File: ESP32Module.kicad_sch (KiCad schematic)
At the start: 5 parts, among them U4 ESP32-WROOM-32

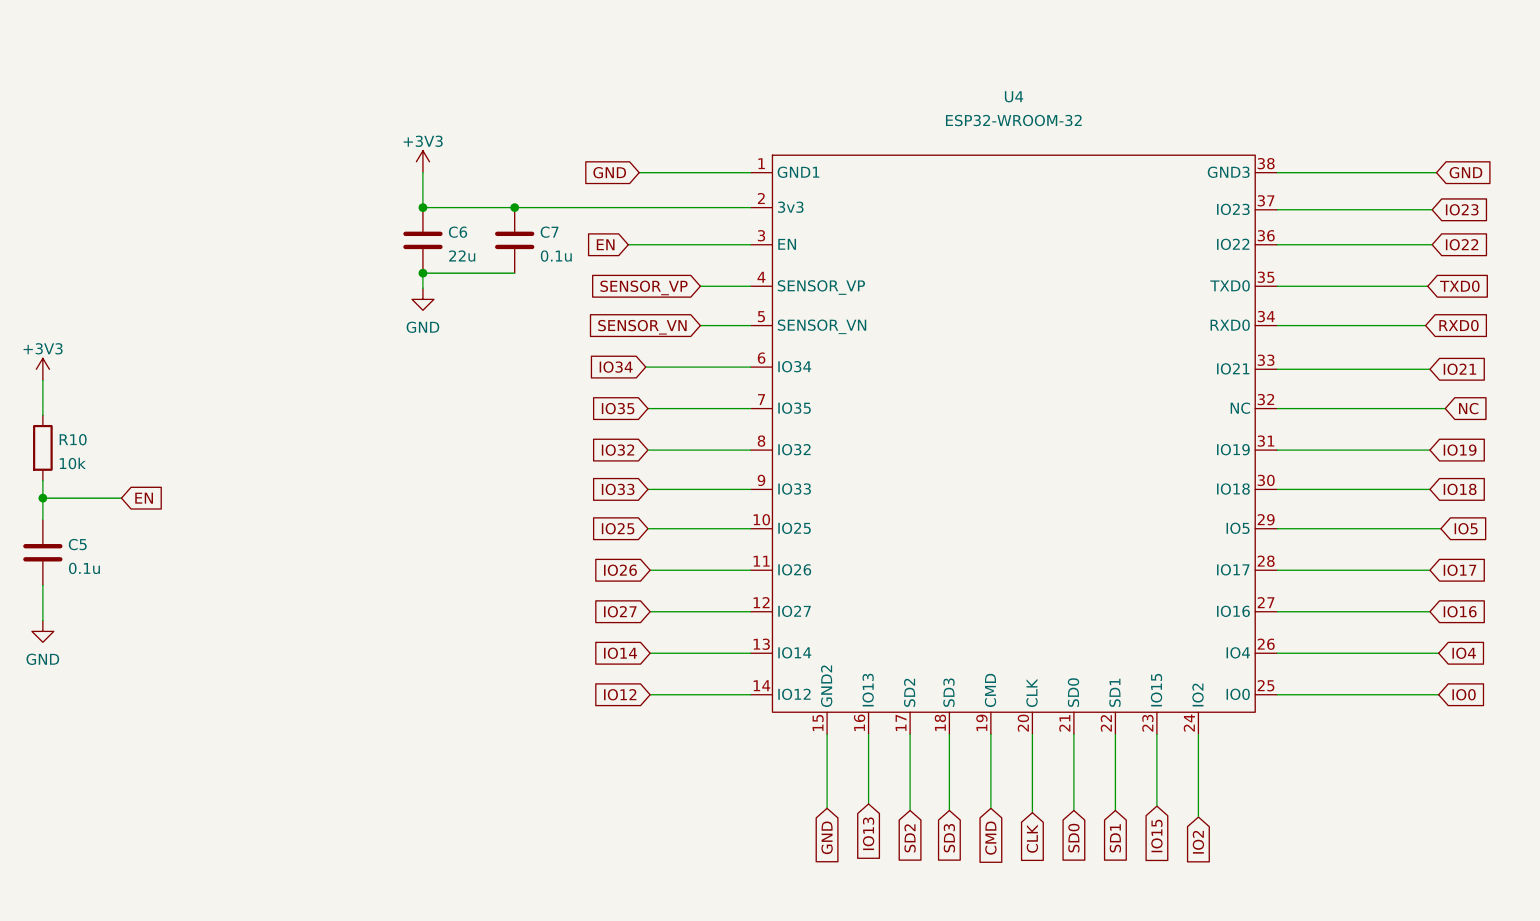
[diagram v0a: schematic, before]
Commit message: Added VOC and Optical Sensors
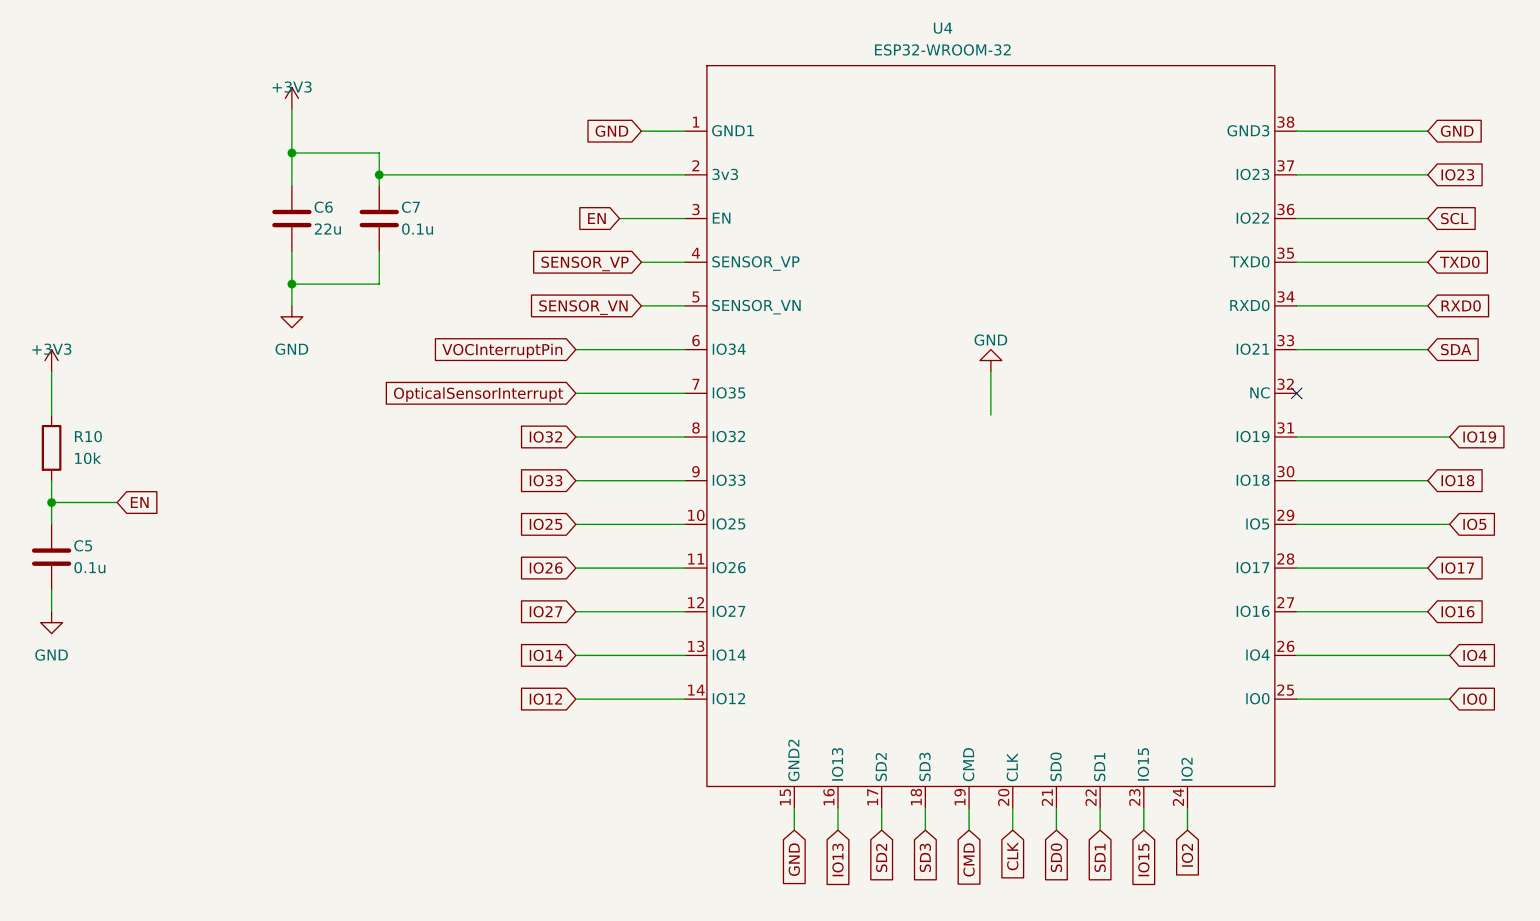
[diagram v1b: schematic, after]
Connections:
- net GND: now also U4.1.1 (P_GND)
- net IO21 renamed SDA
- net IO22 renamed SCL
- net IO34 renamed VOCInterruptPin
- net IO35 renamed OpticalSensorInterrupt
- net NC: no longer names the net of U4.32 (NC)
- no-connect marks 0 -> 1
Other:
- moved on the sheet: C5, C6, C7, R10, U4

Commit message: Vertical Horizontal Traces
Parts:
- R10: footprint Resistor_SMD:R_0603_1608Metric -> Resistor_SMD:R_0603_1608Metric_Pad0.98x0.95mm_HandSolder
- U4: footprint ESP-WROOM-32:MODULE_ESP-WROOM-32 -> ESP32-WROOM-32:MODULE_ESP-WROOM-32
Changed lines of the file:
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@@
       (effects (font (size 1.27 1.27)) (justify left))
     )
-    (property "Footprint" "Resistor_SMD:R_0603_1608Metric" (id 2) (at 41.402 105.41 90)
+    (property "Footprint" "Resistor_SMD:R_0603_1608Metric_Pad0.98x0.95mm_HandSolder" (id 2) (at 41.402 105.41 90)
       (effects (font (size 1.27 1.27)) hide)
     )
@@
     (property "Reference" "U4" (id 0) (at 146.812 56.642 0))
     (property "Value" "ESP32-WROOM-32" (id 1) (at 146.812 59.182 0))
-    (property "Footprint" "ESP-WROOM-32:MODULE_ESP-WROOM-32" (id 2) (at 165.1 22.86 0)
+    (property "Footprint" "ESP32-WROOM-32:MODULE_ESP-WROOM-32" (id 2) (at 165.1 22.86 0)
       (effects (font (size 1.27 1.27)) hide)
     )
